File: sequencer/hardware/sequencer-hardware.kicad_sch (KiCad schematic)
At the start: 49 parts, among them J1 Barrel Jack, J2 40Pin 0.1", J3 USB_B_Micro, J4 Conn_01x02_Male, J5 JST 4-Pin male, J6 TS Out, SW1 PWR, SW2 SW_Push, U1 L7805_A, U2 L7805_D, U3 ICL7660, U4 NCP1117-3.3_TO252, U5 OPA703UA, U6 OPA703UA

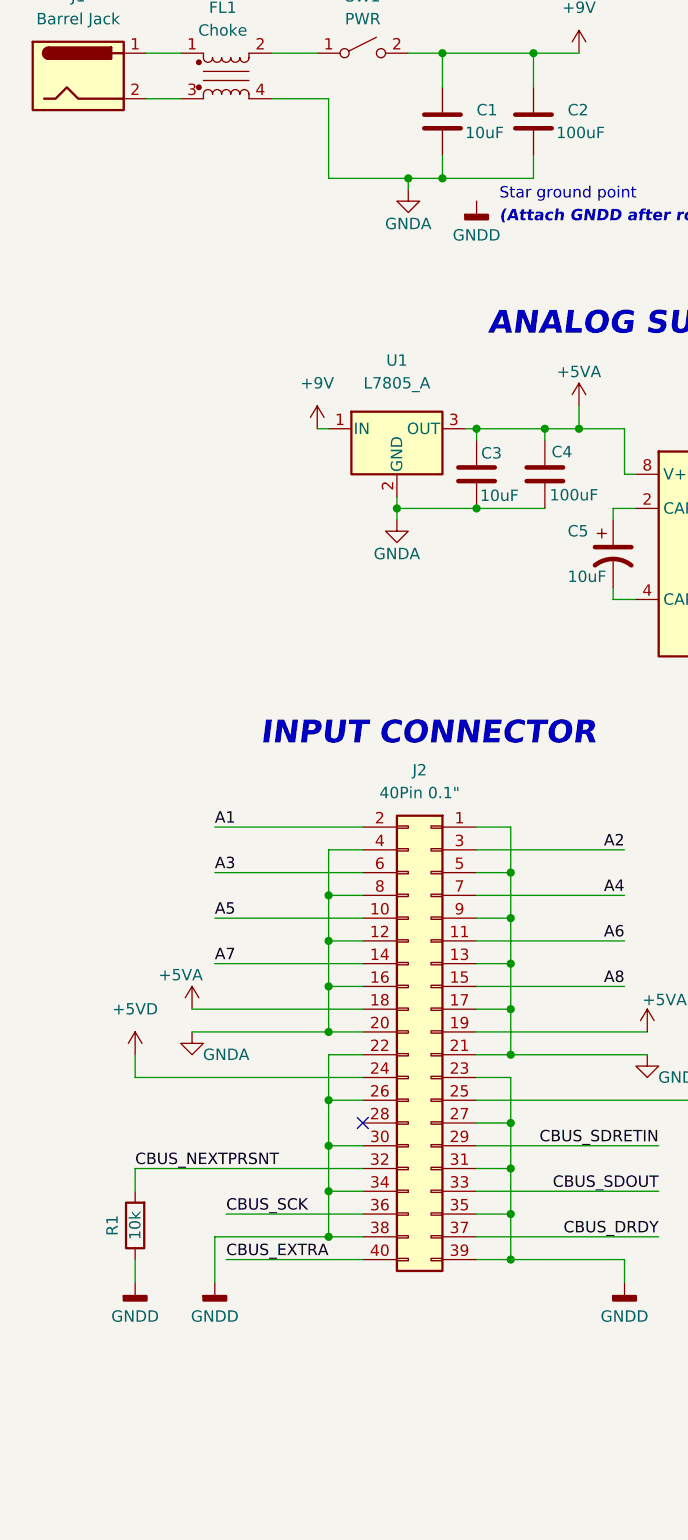
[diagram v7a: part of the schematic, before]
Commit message: add mounting holes, arrange all parts
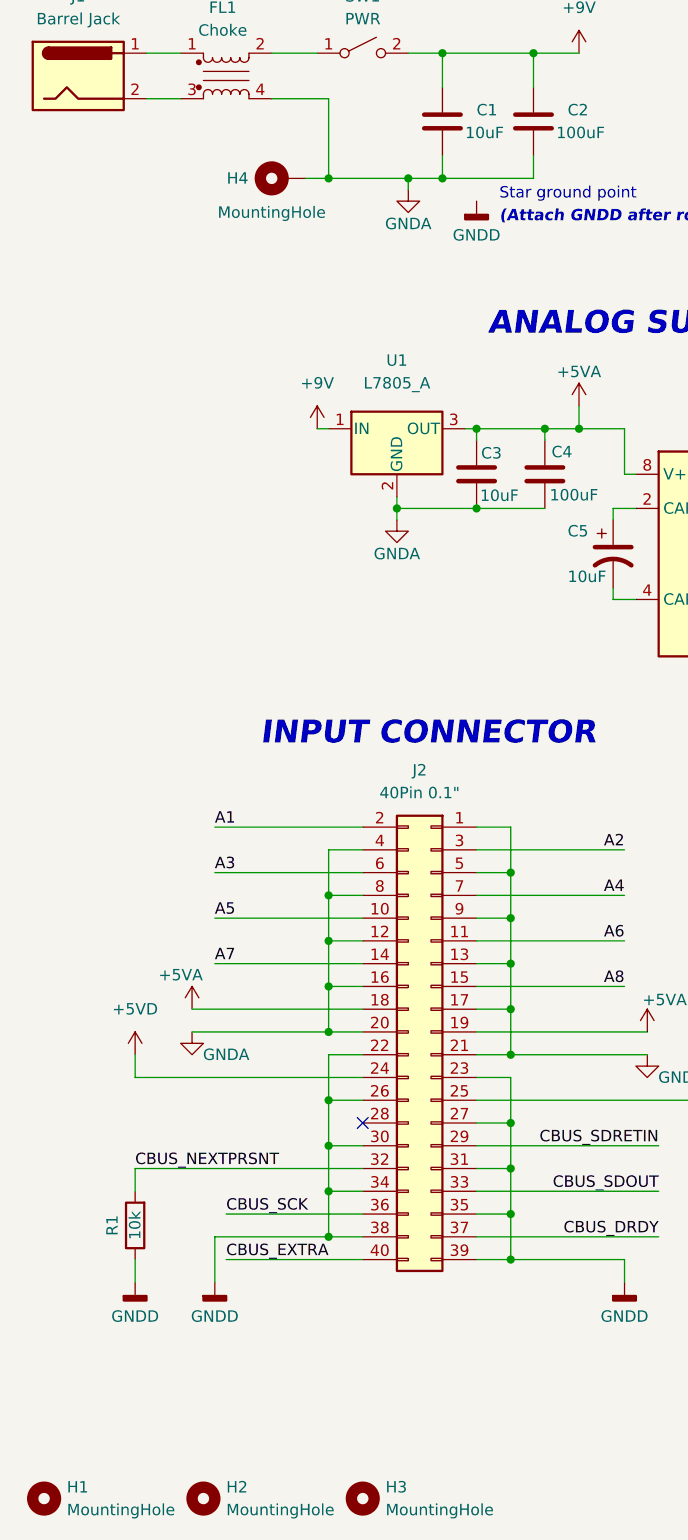
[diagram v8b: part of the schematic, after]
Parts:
- added H1, H2, H3: MountingHole, MountingHole:MountingHole_3.2mm_M3_ISO14580, symbol Mechanical:MountingHole
- added H4: MountingHole, MountingHole:MountingHole_3.2mm_M3_ISO14580_Pad, symbol Mechanical:MountingHole_Pad
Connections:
- net GNDA: now also H4.1
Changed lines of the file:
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@@
   (junction (at 48.26 147.32) (diameter 0) (color 0 0 0 0)
+  )
+  (junction (at 48.26 52.07) (diameter 0) (color 0 0 0 0)
   )
   (junction (at 60.96 38.1) (diameter 0) (color 0 0 0 0)
@@
     (stroke (width 0) (type default) (color 0 0 0 0))
   )
+  (wire (pts (xy 45.72 52.07) (xy 48.26 52.07))
+    (stroke (width 0) (type default) (color 0 0 0 0))
+  )
   (wire (pts (xy 76.2 77.47) (xy 76.2 80.01))
     (stroke (width 0) (type default) (color 0 0 0 0))
@@
     )
     (property "Datasheet" "" (id 3) (at 237.49 140.97 0)
+      (effects (font (size 1.27 1.27)) hide)
+    )
+    (pin "1")
+  )
+  (symbol (lib_id "Mechanical:MountingHole_Pad") (at 43.18 52.07 90) (unit 1)
+    (in_bom yes) (on_board yes)
+    (property "Reference" "H4" (id 0) (at 38.1 52.07 90))
+    (property "Value" "MountingHole" (id 1) (at 41.91 55.88 90))
+    (property "Footprint" "MountingHole:MountingHole_3.2mm_M3_ISO14580_Pad" (id 2) (at 43.18 52.07 0)
+      (effects (font (size 1.27 1.27)) hide)
+    )
+    (property "Datasheet" "~" (id 3) (at 43.18 52.07 0)
       (effects (font (size 1.27 1.27)) hide)
     )
@@
     (pin "4")
   )
+  (symbol (lib_id "Mechanical:MountingHole") (at 52.07 199.39 0) (unit 1)
+    (in_bom yes) (on_board yes) (fields_autoplaced)
+    (property "Reference" "H3" (id 0) (at 54.61 198.1199 0)
+      (effects (font (size 1.27 1.27)) (justify left))
+    )
+    (property "Value" "MountingHole" (id 1) (at 54.61 200.6599 0)
+      (effects (font (size 1.27 1.27)) (justify left))
+    )
+    (property "Footprint" "MountingHole:MountingHole_3.2mm_M3_ISO14580" (id 2) (at 52.07 199.39 0)
+      (effects (font (size 1.27 1.27)) hide)
+    )
+    (property "Datasheet" "~" (id 3) (at 52.07 199.39 0)
+      (effects (font (size 1.27 1.27)) hide)
+    )
+  )
   (symbol (lib_id "Device:C_Polarized_US") (at 105.41 93.98 0) (unit 1)
     (in_bom yes) (on_board yes)
@@
     (pin "1")
     (pin "2")
+  )
+  (symbol (lib_id "Mechanical:MountingHole") (at 16.51 199.39 0) (unit 1)
+    (in_bom yes) (on_board yes) (fields_autoplaced)
+    (property "Reference" "H1" (id 0) (at 19.05 198.1199 0)
+      (effects (font (size 1.27 1.27)) (justify left))
+    )
+    (property "Value" "MountingHole" (id 1) (at 19.05 200.6599 0)
+      (effects (font (size 1.27 1.27)) (justify left))
+    )
+    (property "Footprint" "MountingHole:MountingHole_3.2mm_M3_ISO14580" (id 2) (at 16.51 199.39 0)
+      (effects (font (size 1.27 1.27)) hide)
+    )
+    (property "Datasheet" "~" (id 3) (at 16.51 199.39 0)
+      (effects (font (size 1.27 1.27)) hide)
+    )
   )
   (symbol (lib_id "Switch:SW_Push") (at 163.83 114.3 0) (unit 1)
@@
     (pin "1")
   )
+  (symbol (lib_id "Mechanical:MountingHole") (at 34.29 199.39 0) (unit 1)
+    (in_bom yes) (on_board yes) (fields_autoplaced)
+    (property "Reference" "H2" (id 0) (at 36.83 198.1199 0)
+      (effects (font (size 1.27 1.27)) (justify left))
+    )
+    (property "Value" "MountingHole" (id 1) (at 36.83 200.6599 0)
+      (effects (font (size 1.27 1.27)) (justify left))
+    )
+    (property "Footprint" "MountingHole:MountingHole_3.2mm_M3_ISO14580" (id 2) (at 34.29 199.39 0)
+      (effects (font (size 1.27 1.27)) hide)
+    )
+    (property "Datasheet" "~" (id 3) (at 34.29 199.39 0)
+      (effects (font (size 1.27 1.27)) hide)
+    )
+  )
   (symbol (lib_id "power:+3.3V") (at 312.42 34.29 0) (unit 1)
     (in_bom yes) (on_board yes)
@@
       (reference "FL1") (unit 1) (value "Choke") (footprint "Inductor_THT:Choke_Schaffner_RN102-04-14.0x14.0mm")
     )
+    (path "/cec2d5fe-b6d2-4577-baa7-d0df8627af85"
+      (reference "H1") (unit 1) (value "MountingHole") (footprint "MountingHole:MountingHole_3.2mm_M3_ISO14580")
+    )
+    (path "/ebf4e07a-18af-4911-99ec-e9693de60368"
+      (reference "H2") (unit 1) (value "MountingHole") (footprint "MountingHole:MountingHole_3.2mm_M3_ISO14580")
+    )
+    (path "/6b879a06-9650-477a-9c9b-0d395d5799c1"
+      (reference "H3") (unit 1) (value "MountingHole") (footprint "MountingHole:MountingHole_3.2mm_M3_ISO14580")
+    )
+    (path "/243b3c1b-99cb-43f6-8b26-159acfcb9aa0"
+      (reference "H4") (unit 1) (value "MountingHole") (footprint "MountingHole:MountingHole_3.2mm_M3_ISO14580_Pad")
+    )
     (path "/e7d77e35-7d0f-418c-bddb-e70c65e01157"
